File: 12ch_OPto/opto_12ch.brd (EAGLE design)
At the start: 66 parts, among them J1 RJMG2310228A0ER, J2 RJMG2310228A0ER, U10 PCF8575PWRE4, U19 MOC3063S, U20 MOC3063S, U21 MOC3063S, U22 MOC3063S, U23 MOC3063S, U24 MOC3063S, U25 MOC3063S, U26 MOC3063S, U27 LM317, U29 Z0103MN, U30 Z0103MN, U31 Z0103MN, U32 Z0103MN, U33 Z0103MN, U34 Z0103MN, U35 Z0103MN, U36 Z0103MN, X1 TSW-101-07-G-D

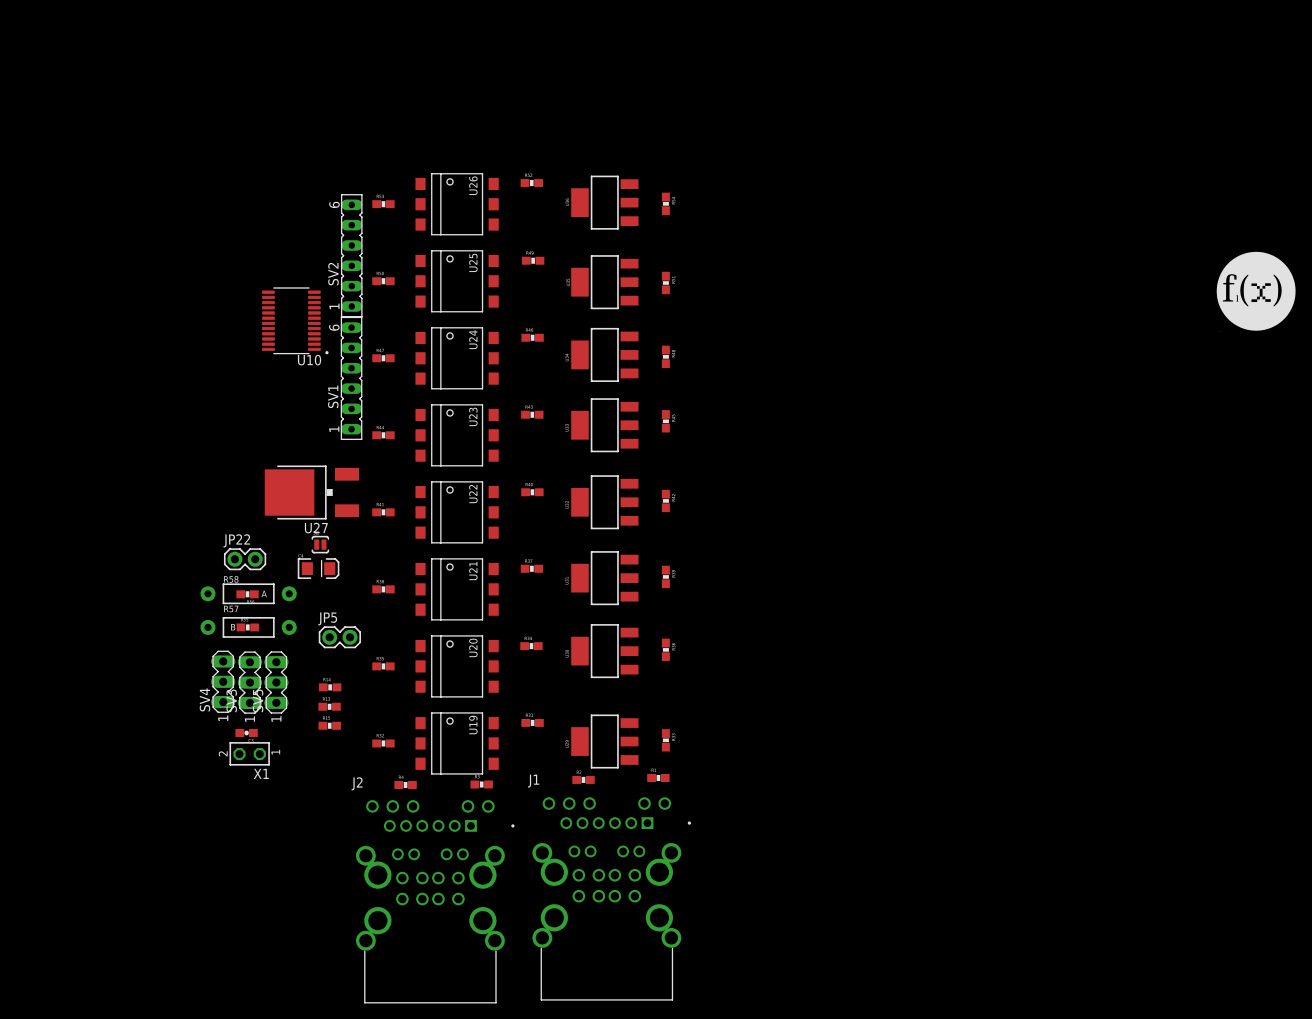
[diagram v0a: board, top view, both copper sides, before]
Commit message: optimiz
Se redujo lo mayor posible las dimensiones de la placa
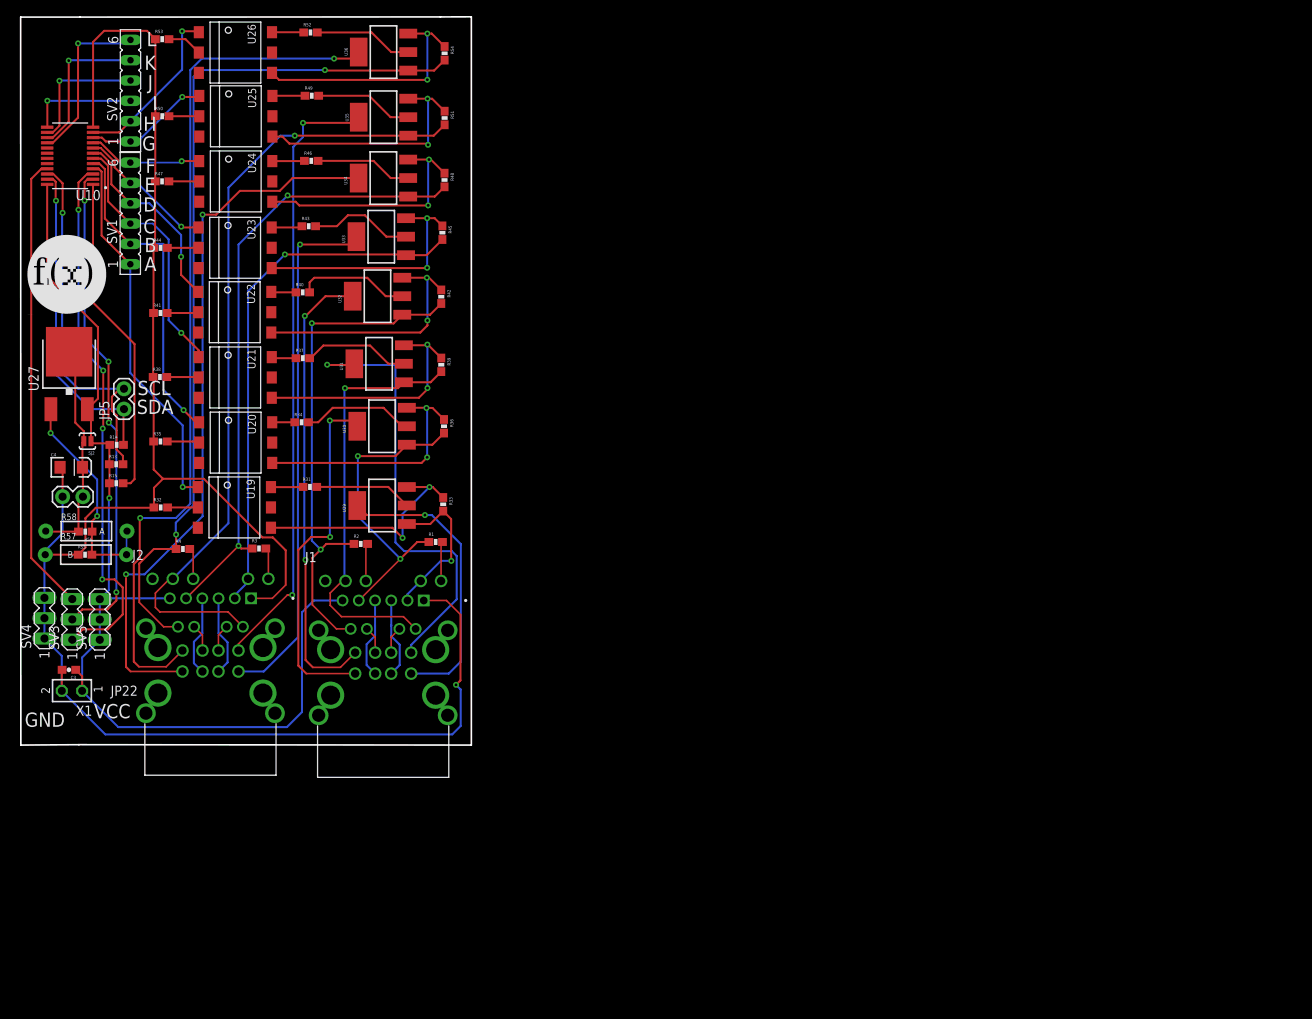
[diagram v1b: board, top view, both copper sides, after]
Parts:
- moved R32 40.6 mm to (16.7, 34.2)
- moved U29 40.6 mm to (44.4, 34.4)
- moved R2 40.6 mm to (41.7, 29.6)
- moved R3 40.6 mm to (29.0, 29.1)
- moved R31 40.6 mm to (35.3, 36.8)
- moved R4 40.6 mm to (19.5, 29.0)
- moved U19 40.6 mm to (25.9, 34.2)
- moved R1 40.6 mm to (51.1, 29.9)
- moved R33 40.6 mm to (52.0, 34.6)
- moved R13 40.4 mm to (11.1, 39.6)
- moved R14 40.4 mm to (11.2, 42.0)
- moved R15 40.4 mm to (11.1, 37.2)
- moved R34 40.1 mm to (34.3, 44.8)
- moved R35 39.6 mm to (16.6, 42.4)
- moved J2 39.6 mm to (22.9, 16.7)
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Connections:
- net N$21 renamed SCL
- net N$22 renamed SDA
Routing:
- net GND: track 0.00 -> 230.5 mm, vias 0 -> 1
- net VCC: track 0.00 -> 130.3 mm, vias 0 -> 1
- net GND4: track 0.00 -> 108.6 mm, vias 0 -> 2
- net TR4: track 0.00 -> 108.6 mm, vias 0 -> 2
- net PO4: track 0.00 -> 98.7 mm, vias 0 -> 1
- net GND3: track 0.00 -> 90.5 mm, vias 0 -> 2
- net TR3: track 0.00 -> 77.6 mm, vias 0 -> 2
- net POWER4: track 0.00 -> 76.9 mm, vias 0 -> 2
- net N$25: track 0.00 -> 67.2 mm, vias 0 -> 4
- net PO3: track 0.00 -> 66.1 mm, vias 0 -> 1
- net POWER3: track 0.00 -> 65.9 mm, vias 0 -> 1
- net TR2: track 0.00 -> 63.8 mm, vias 0 -> 2
- net N$24: track 0.00 -> 61.7 mm, vias 0 -> 4
- net GND2: track 0.00 -> 57.5 mm, vias 0 -> 2
- net N$23: track 0.00 -> 57.2 mm
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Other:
- board outline added: 56.3 x 91 mm
- board text added: "A"
- board text added: "B"
- board text added: "C"
- board text added: "D"
- board text added: "E"
- board text added: "F"
- board text added: "G"
- board text added: "GND"
- board text added: "H"
- board text added: "I"
- board text added: "J"
- board text added: "K"
- board text added: "L"
- board text added: "SCL"
- board text added: "SDA"
- board text added: "VCC"
- board text added: "www.flatbox.co"
